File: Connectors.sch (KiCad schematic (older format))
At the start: 16 parts

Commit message: Design Mic. Board
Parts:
- added J?: JST-PH, symbol Connector_Generic:Conn_01x02
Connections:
- net GND: now also J?.2 (Pin_2)
- new net +BATT: J?.1 (Pin_1)
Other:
- note added: "LIPO Battery Connector"
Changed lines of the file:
@@
 $Descr A4 11693 8268
 encoding utf-8
-Sheet 13 13
+Sheet 13 14
 Title ""
 Date ""
@@
 Text Notes 750  3100 0    50   ~ 10
 SD Card Holder
+$Comp
+L Connector_Generic:Conn_01x02 J?
+U 1 1 5EE0C945
+P 6400 1450
+F 0 "J?" H 6480 1442 50  0000 L CNN
+F 1 "JST-PH" H 6480 1351 50  0000 L CNN
+F 2 "" H 6400 1450 50  0001 C CNN
+F 3 "~" H 6400 1450 50  0001 C CNN
+	1    6400 1450
+	1    0    0    -1
+$EndComp
+$Comp
+L power:+BATT #PWR?
+U 1 1 5EE0C94B
+P 6200 1250
+F 0 "#PWR?" H 6200 1100 50  0001 C CNN
+F 1 "+BATT" H 6215 1423 50  0000 C CNN
+F 2 "" H 6200 1250 50  0001 C CNN
+F 3 "" H 6200 1250 50  0001 C CNN
+	1    6200 1250
+	1    0    0    -1
+$EndComp
+$Comp
+L power:GND #PWR?
+U 1 1 5EE0C951
+P 6200 1750
+F 0 "#PWR?" H 6200 1500 50  0001 C CNN
+F 1 "GND" H 6205 1577 50  0000 C CNN
+F 2 "" H 6200 1750 50  0001 C CNN
+F 3 "" H 6200 1750 50  0001 C CNN
+	1    6200 1750
+	1    0    0    -1
+$EndComp
+Wire Wire Line
+	6200 1750 6200 1550
+Wire Wire Line
+	6200 1450 6200 1250
+Wire Notes Line
+	5950 2050 6900 2050
+Wire Notes Line
+	6900 2050 6900 950
+Wire Notes Line
+	6900 950  5950 950
+Wire Notes Line
+	5950 950  5950 2050
+Text Notes 5950 950  0    50   ~ 10
+LIPO Battery Connector
 $EndSCHEMATC

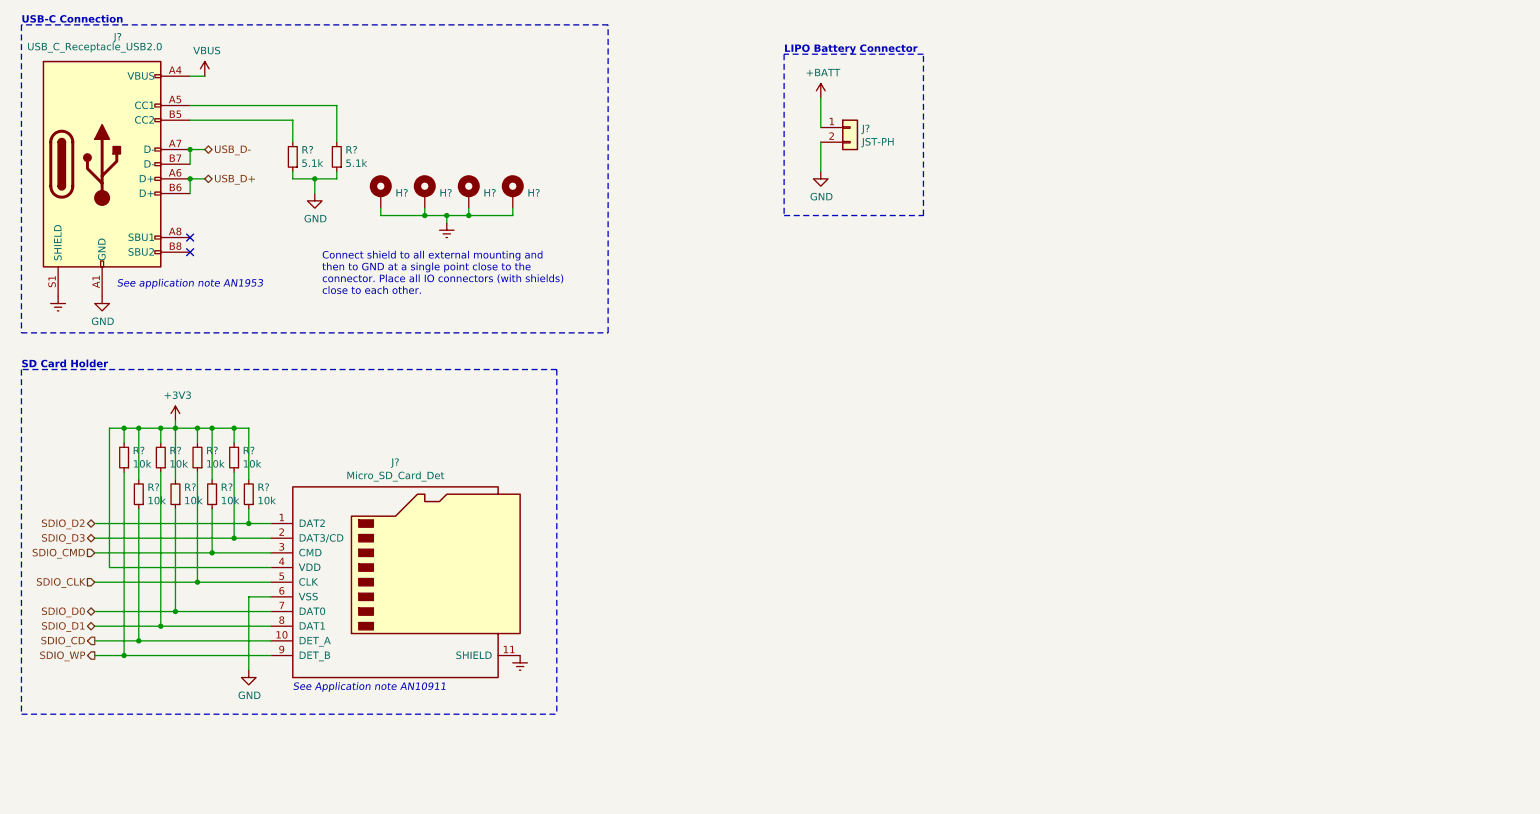
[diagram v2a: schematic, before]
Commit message: Design MCU section
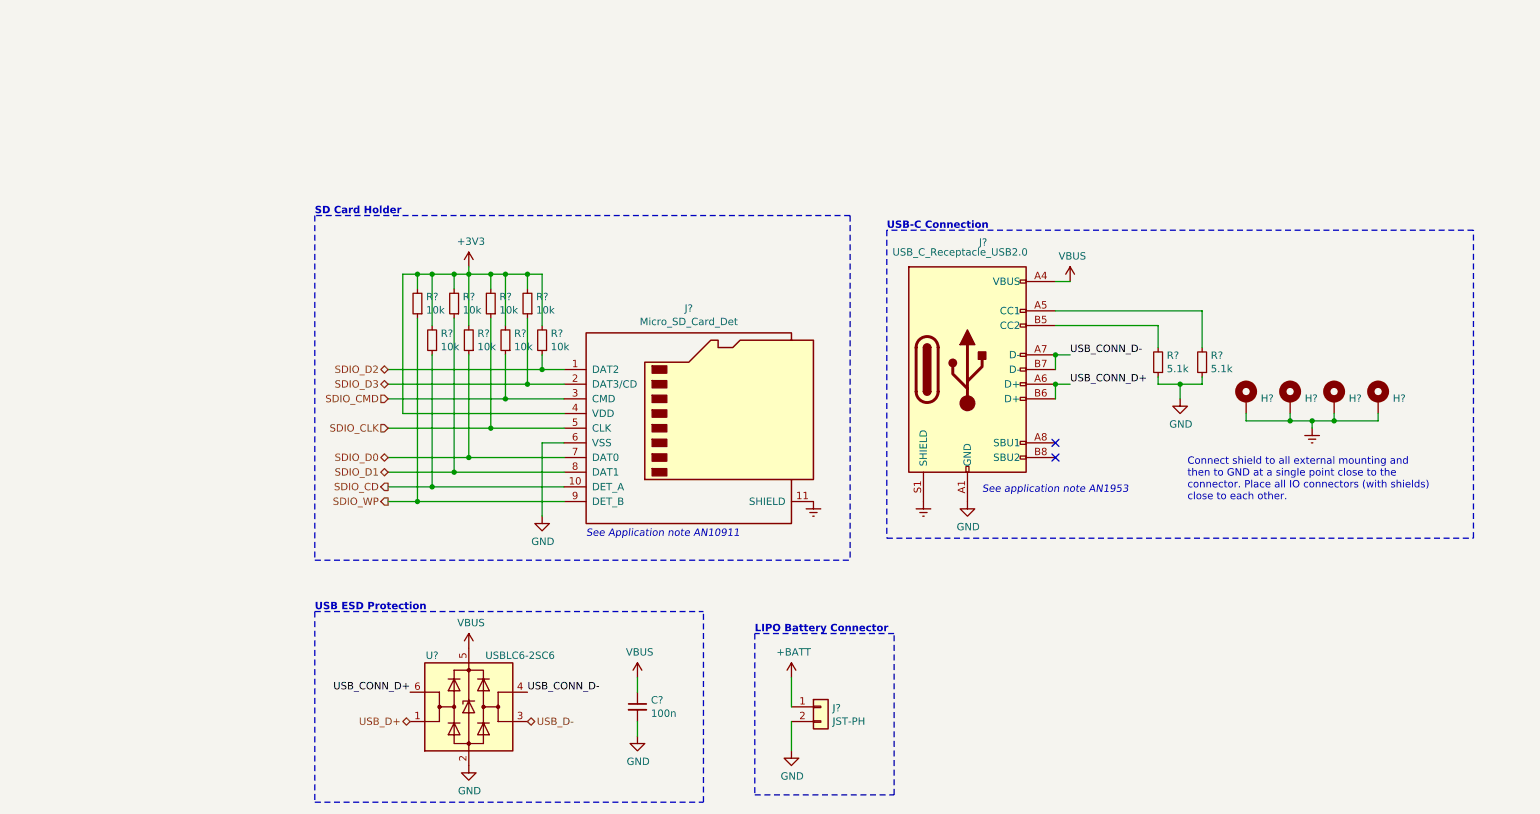
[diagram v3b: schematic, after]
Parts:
- added C?: 100n, symbol Device:C_Small
- added U?: USBLC6-2SC6, Package_TO_SOT_SMD:SOT-23-6, symbol Power_Protection:USBLC6-2SC6
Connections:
- net GND: now also C?.2, U?.2 (GND)
- net USB_D+: now also U?.1 (I/O1); no longer J?.A6 (D+), J?.B6 (D+)
- net USB_D-: now also U?.3 (I/O2); no longer J?.A7 (D-), J?.B7 (D-)
- net VBUS: now also C?.1, U?.5 (VBUS)
- new net USB_CONN_D+: J?.A6 (D+), J?.B6 (D+), U?.6 (I/O1)
- new net USB_CONN_D-: J?.A7 (D-), J?.B7 (D-), U?.4 (I/O2)
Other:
- note added: "USB ESD Protection"
- moved on the sheet: H?, J?, R?

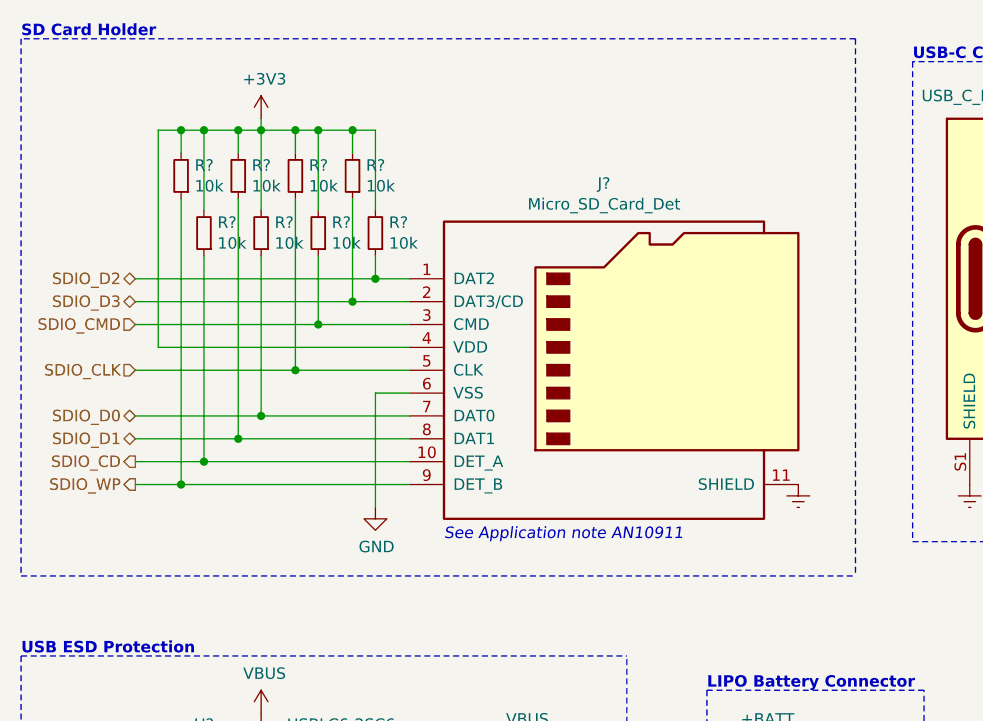
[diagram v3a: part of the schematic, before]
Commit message: Remove SD pullup resistors
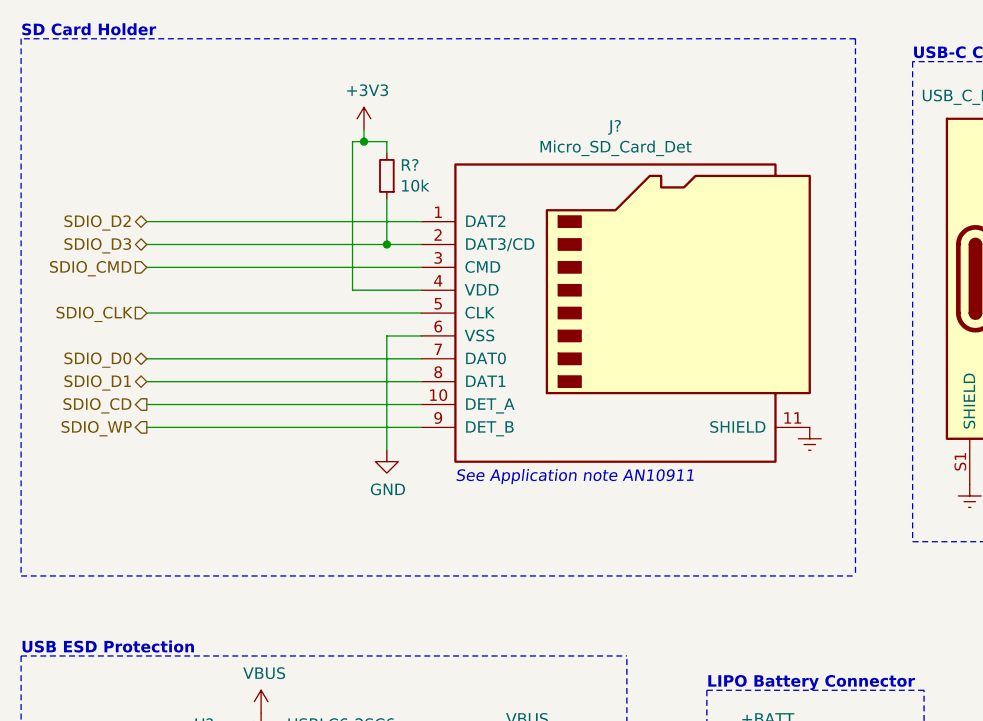
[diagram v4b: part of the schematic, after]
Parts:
- removed R? (x7): 10k, symbol Device:R_Small
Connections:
- net SDIO_D2: no longer R?.1
- net SDIO_D3: now also R?.1
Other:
- moved on the sheet: J?, R?

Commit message: Add PWR Flags
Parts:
- gave numbers to parts that had none: 12
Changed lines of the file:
@@
 $EndDescr
 $Comp
-L power:GND #PWR?
+L power:GND #PWR095
 U 1 1 5EF579E9
 P 7200 4000
-F 0 "#PWR?" H 7200 3750 50  0001 C CNN
+F 0 "#PWR095" H 7200 3750 50  0001 C CNN
 F 1 "GND" H 7205 3827 50  0000 C CNN
 F 2 "" H 7200 4000 50  0001 C CNN
@@
 $EndComp
 $Comp
-L power:Earth #PWR?
+L power:Earth #PWR094
 U 1 1 5EF579EF
 P 6900 4000
-F 0 "#PWR?" H 6900 3750 50  0001 C CNN
+F 0 "#PWR094" H 6900 3750 50  0001 C CNN
 F 1 "Earth" H 6900 3850 50  0001 C CNN
 F 2 "" H 6900 4000 50  0001 C CNN
@@
 $EndComp
 $Comp
-L power:VBUS #PWR?
+L power:VBUS #PWR096
 U 1 1 5EF579F5
 P 7900 2500
-F 0 "#PWR?" H 7900 2350 50  0001 C CNN
+F 0 "#PWR096" H 7900 2350 50  0001 C CNN
 F 1 "VBUS" H 7915 2673 50  0000 C CNN
 F 2 "" H 7900 2500 50  0001 C CNN
@@
 	7900 3000 7800 3000
 $Comp
-L Connector:USB_C_Receptacle_USB2.0 J?
+L Connector:USB_C_Receptacle_USB2.0 J11
 U 1 1 5EF57A02
 P 7200 3100
-F 0 "J?" H 7307 3967 50  0000 C CNN
+F 0 "J11" H 7307 3967 50  0000 C CNN
 F 1 "USB_C_Receptacle_USB2.0" H 7150 3900 50  0000 C CNN
 F 2 "" H 7350 3100 50  0001 C CNN
@@
 NoConn ~ 7800 3600
 $Comp
-L Device:R_Small R?
+L Device:R_Small R54
 U 1 1 5EF57A0A
 P 8500 3050
-F 0 "R?" H 8441 3004 50  0000 R CNN
+F 0 "R54" H 8441 3004 50  0000 R CNN
 F 1 "5.1k" H 8441 3095 50  0000 R CNN
 F 2 "" H 8500 3050 50  0001 C CNN
@@
 $EndComp
 $Comp
-L Device:R_Small R?
+L Device:R_Small R55
 U 1 1 5EF57A10
 P 8800 3050
-F 0 "R?" H 8741 3004 50  0000 R CNN
+F 0 "R55" H 8741 3004 50  0000 R CNN
 F 1 "5.1k" H 8741 3095 50  0000 R CNN
 F 2 "" H 8800 3050 50  0001 C CNN
@@
 	8800 2700 7800 2700
 $Comp
-L power:GND #PWR?
+L power:GND #PWR097
 U 1 1 5EF57A1A
 P 8650 3300
-F 0 "#PWR?" H 8650 3050 50  0001 C CNN
+F 0 "#PWR097" H 8650 3050 50  0001 C CNN
 F 1 "GND" H 8655 3127 50  0000 C CNN
 F 2 "" H 8650 3300 50  0001 C CNN
@@
 	9550 3500 9550 3450
 $Comp
-L power:Earth #PWR?
+L power:Earth #PWR098
 U 1 1 5EF57A38
 P 9550 3500
-F 0 "#PWR?" H 9550 3250 50  0001 C CNN
+F 0 "#PWR098" H 9550 3250 50  0001 C CNN
 F 1 "Earth" H 9550 3350 50  0001 C CNN
 F 2 "" H 9550 3500 50  0001 C CNN
@@
 $EndComp
 $Comp
-L Mechanical:MountingHole_Pad H?
+L Mechanical:MountingHole_Pad H4
 U 1 1 5EF57A3E
 P 10000 3300
-F 0 "H?" H 10100 3303 50  0000 L CNN
+F 0 "H4" H 10100 3303 50  0000 L CNN
 F 1 "MountingHole_Pad" H 10100 3258 50  0001 L CNN
 F 2 "" H 10000 3300 50  0001 C CNN
@@
 $EndComp
 $Comp
-L Mechanical:MountingHole_Pad H?
+L Mechanical:MountingHole_Pad H3
 U 1 1 5EF57A44
 P 9700 3300
-F 0 "H?" H 9800 3303 50  0000 L CNN
+F 0 "H3" H 9800 3303 50  0000 L CNN
 F 1 "MountingHole_Pad" H 9800 3258 50  0001 L CNN
 F 2 "" H 9700 3300 50  0001 C CNN
@@
 $EndComp
 $Comp
-L Mechanical:MountingHole_Pad H?
+L Mechanical:MountingHole_Pad H2
 U 1 1 5EF57A4A
 P 9400 3300
-F 0 "H?" H 9500 3303 50  0000 L CNN
+F 0 "H2" H 9500 3303 50  0000 L CNN
 F 1 "MountingHole_Pad" H 9500 3258 50  0001 L CNN
 F 2 "" H 9400 3300 50  0001 C CNN
@@
 $EndComp
 $Comp
-L Mechanical:MountingHole_Pad H?
+L Mechanical:MountingHole_Pad H1
 U 1 1 5EF57A50
 P 9100 3300
-F 0 "H?" H 9200 3303 50  0000 L CNN
+F 0 "H1" H 9200 3303 50  0000 L CNN
 F 1 "MountingHole_Pad" H 9200 3258 50  0001 L CNN
 F 2 "" H 9100 3300 50  0001 C CNN
@@
 USB-C Connection
 $Comp
-L power:Earth #PWR?
+L power:Earth #PWR093
 U 1 1 5EF59730
 P 6200 3750
-F 0 "#PWR?" H 6200 3500 50  0001 C CNN
+F 0 "#PWR093" H 6200 3500 50  0001 C CNN
 F 1 "Earth" H 6200 3600 50  0001 C CNN
 F 2 "" H 6200 3750 50  0001 C CNN
@@
 SDIO_WP
 $Comp
-L power:GND #PWR?
+L power:GND #PWR088
 U 1 1 5EFBCDAD
 P 4350 3850
-F 0 "#PWR?" H 4350 3600 50  0001 C CNN
+F 0 "#PWR088" H 4350 3600 50  0001 C CNN
 F 1 "GND" H 4355 3677 50  0000 C CNN
 F 2 "" H 4350 3850 50  0001 C CNN
@@
 SD Card Holder
 $Comp
-L Connector_Generic:Conn_01x02 J?
+L Connector_Generic:Conn_01x02 J10
 U 1 1 5EE0C945
 P 6200 5400
-F 0 "J?" H 6280 5392 50  0000 L CNN
+F 0 "J10" H 6280 5392 50  0000 L CNN
 F 1 "JST-PH" H 6280 5301 50  0000 L CNN
 F 2 "" H 6200 5400 50  0001 C CNN
@@
 $EndComp
 $Comp
-L power:+BATT #PWR?
+L power:+BATT #PWR091
 U 1 1 5EE0C94B
 P 6000 5200
-F 0 "#PWR?" H 6000 5050 50  0001 C CNN
+F 0 "#PWR091" H 6000 5050 50  0001 C CNN
 F 1 "+BATT" H 6015 5373 50  0000 C CNN
 F 2 "" H 6000 5200 50  0001 C CNN
@@
 $EndComp
 $Comp
-L power:GND #PWR?
+L power:GND #PWR092
 U 1 1 5EE0C951
 P 6000 5700
-F 0 "#PWR?" H 6000 5450 50  0001 C CNN
+F 0 "#PWR092" H 6000 5450 50  0001 C CNN
 F 1 "GND" H 6005 5527 50  0000 C CNN
 F 2 "" H 6000 5700 50  0001 C CNN
@@
 LIPO Battery Connector
 $Comp
-L Power_Protection:USBLC6-2SC6 U?
+L Power_Protection:USBLC6-2SC6 U8
 U 1 1 5EF91333
 P 3800 5400
-F 0 "U?" H 3550 5750 50  0000 C CNN
+F 0 "U8" H 3550 5750 50  0000 C CNN
 F 1 "USBLC6-2SC6" H 4150 5750 50  0000 C CNN
 F 2 "Package_TO_SOT_SMD:SOT-23-6" H 3800 4900 50  0001 C CNN
@@
 $EndComp
 $Comp
-L power:GND #PWR?
+L power:GND #PWR086
 U 1 1 5EF9E21E
 P 3800 5800
-F 0 "#PWR?" H 3800 5550 50  0001 C CNN
+F 0 "#PWR086" H 3800 5550 50  0001 C CNN
 F 1 "GND" H 3805 5627 50  0000 C CNN
 F 2 "" H 3800 5800 50  0001 C CNN
@@
 $EndComp
 $Comp
-L power:VBUS #PWR?
+L power:VBUS #PWR085
 U 1 1 5EF9EE8C
 P 3800 5000
-F 0 "#PWR?" H 3800 4850 50  0001 C CNN
+F 0 "#PWR085" H 3800 4850 50  0001 C CNN
 F 1 "VBUS" H 3815 5173 50  0000 C CNN
 F 2 "" H 3800 5000 50  0001 C CNN
@@
 USB ESD Protection
 $Comp
-L Device:C_Small C?
+L Device:C_Small C72
 U 1 1 5EFBCA6D
 P 4950 5400
-F 0 "C?" H 5042 5446 50  0000 L CNN
+F 0 "C72" H 5042 5446 50  0000 L CNN
 F 1 "100n" H 5042 5355 50  0000 L CNN
 F 2 "" H 4950 5400 50  0001 C CNN
@@
 $EndComp
 $Comp
-L power:VBUS #PWR?
+L power:VBUS #PWR089
 U 1 1 5EFBD2C9
 P 4950 5200
-F 0 "#PWR?" H 4950 5050 50  0001 C CNN
+F 0 "#PWR089" H 4950 5050 50  0001 C CNN
 F 1 "VBUS" H 4965 5373 50  0000 C CNN
 F 2 "" H 4950 5200 50  0001 C CNN
@@
 $EndComp
 $Comp
-L power:GND #PWR?
+L power:GND #PWR090
 U 1 1 5EFBD729
 P 4950 5600
-F 0 "#PWR?" H 4950 5350 50  0001 C CNN
+F 0 "#PWR090" H 4950 5350 50  0001 C CNN
 F 1 "GND" H 4955 5427 50  0000 C CNN
 F 2 "" H 4950 5600 50  0001 C CNN
@@
 	2750 4750 5400 4750
 $Comp
-L Device:R_Small R?
+L Device:R_Small R53
 U 1 1 5EF7DC5F
 P 4350 2650
-F 0 "R?" H 4291 2604 50  0000 R CNN
+F 0 "R53" H 4291 2604 50  0000 R CNN
 F 1 "10k" H 4291 2695 50  0000 R CNN
 F 2 "" H 4350 2650 50  0001 C CNN
@@
 $EndComp
 $Comp
-L Connector:Micro_SD_Card_Det J?
+L Connector:Micro_SD_Card_Det J9
 U 1 1 5EF580BF
 P 5400 3250
-F 0 "J?" H 5350 4067 50  0000 C CNN
+F 0 "J9" H 5350 4067 50  0000 C CNN
 F 1 "Micro_SD_Card_Det" H 5350 3976 50  0000 C CNN
 F 2 "" H 7450 3950 50  0001 C CNN
@@
 $EndComp
 $Comp
-L power:+3V3 #PWR?
+L power:+3V3 #PWR087
 U 1 1 5EF922F3
 P 4250 2450
-F 0 "#PWR?" H 4250 2300 50  0001 C CNN
+F 0 "#PWR087" H 4250 2300 50  0001 C CNN
 F 1 "+3V3" H 4265 2623 50  0000 C CNN
 F 2 "" H 4250 2450 50  0001 C CNN
